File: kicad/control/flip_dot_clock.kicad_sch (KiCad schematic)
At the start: 36 parts, among them J1 Conn_01x02_Male, J2 Conn_02x08_Odd_Even, J3 Conn_01x05_Male, U1 NUCLEO-F303K8-HEADER, U10 Small_7_Seg_FlipDot_Module, U2 SLC03B-05, U3 NCV7719, U4 Small_7_Seg_FlipDot_Module, U5 NCV7719, U6 Small_7_Seg_FlipDot_Module, U7 NCV7719, U8 Small_7_Seg_FlipDot_Module, U9 NCV7719

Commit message: kicad update
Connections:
- net +5V: now also J2.10 (Pin_10); no longer J2.6 (Pin_6)
- net GND: now also J2.14 (Pin_14); no longer J2.10 (Pin_10)

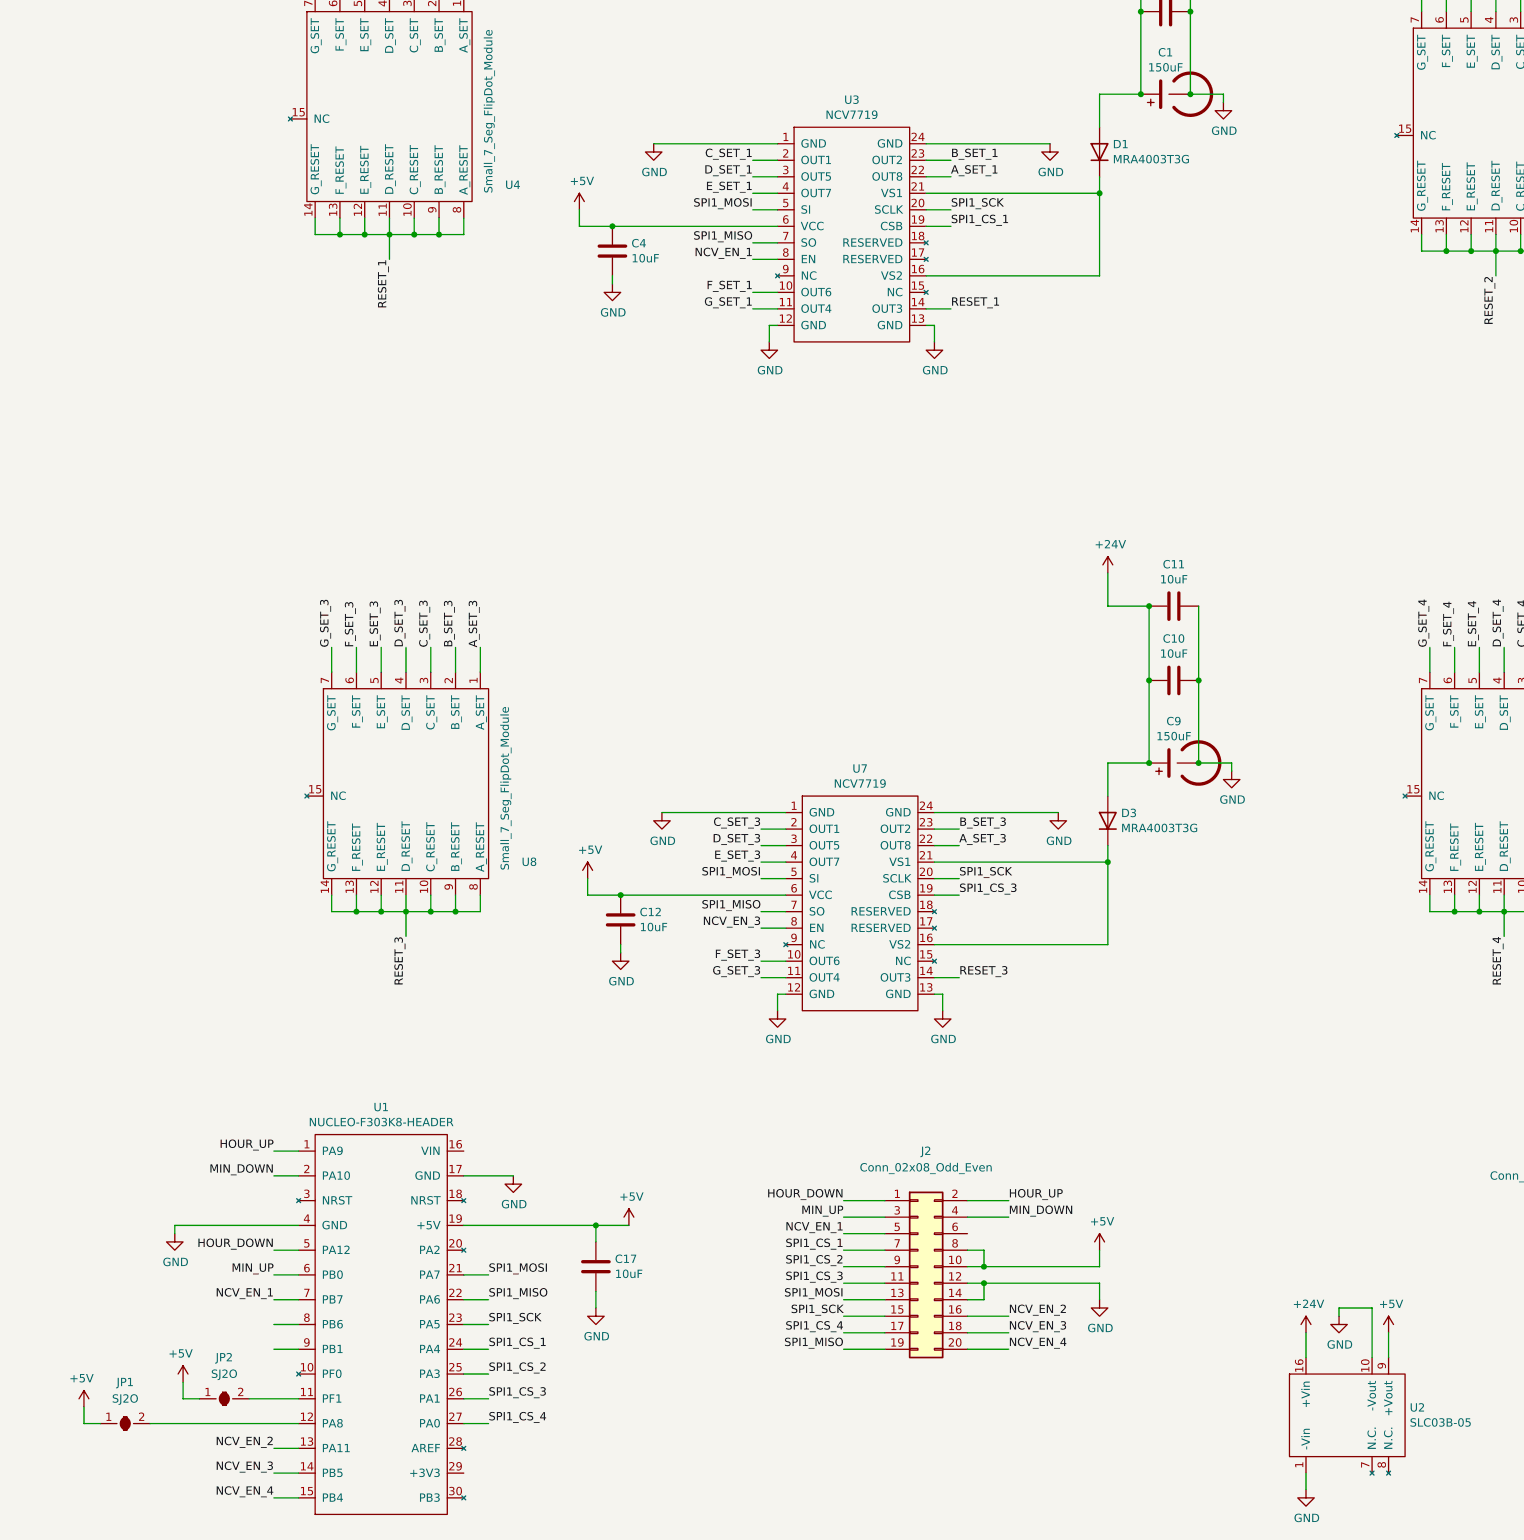
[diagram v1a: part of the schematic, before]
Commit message: add digit holder ground planes
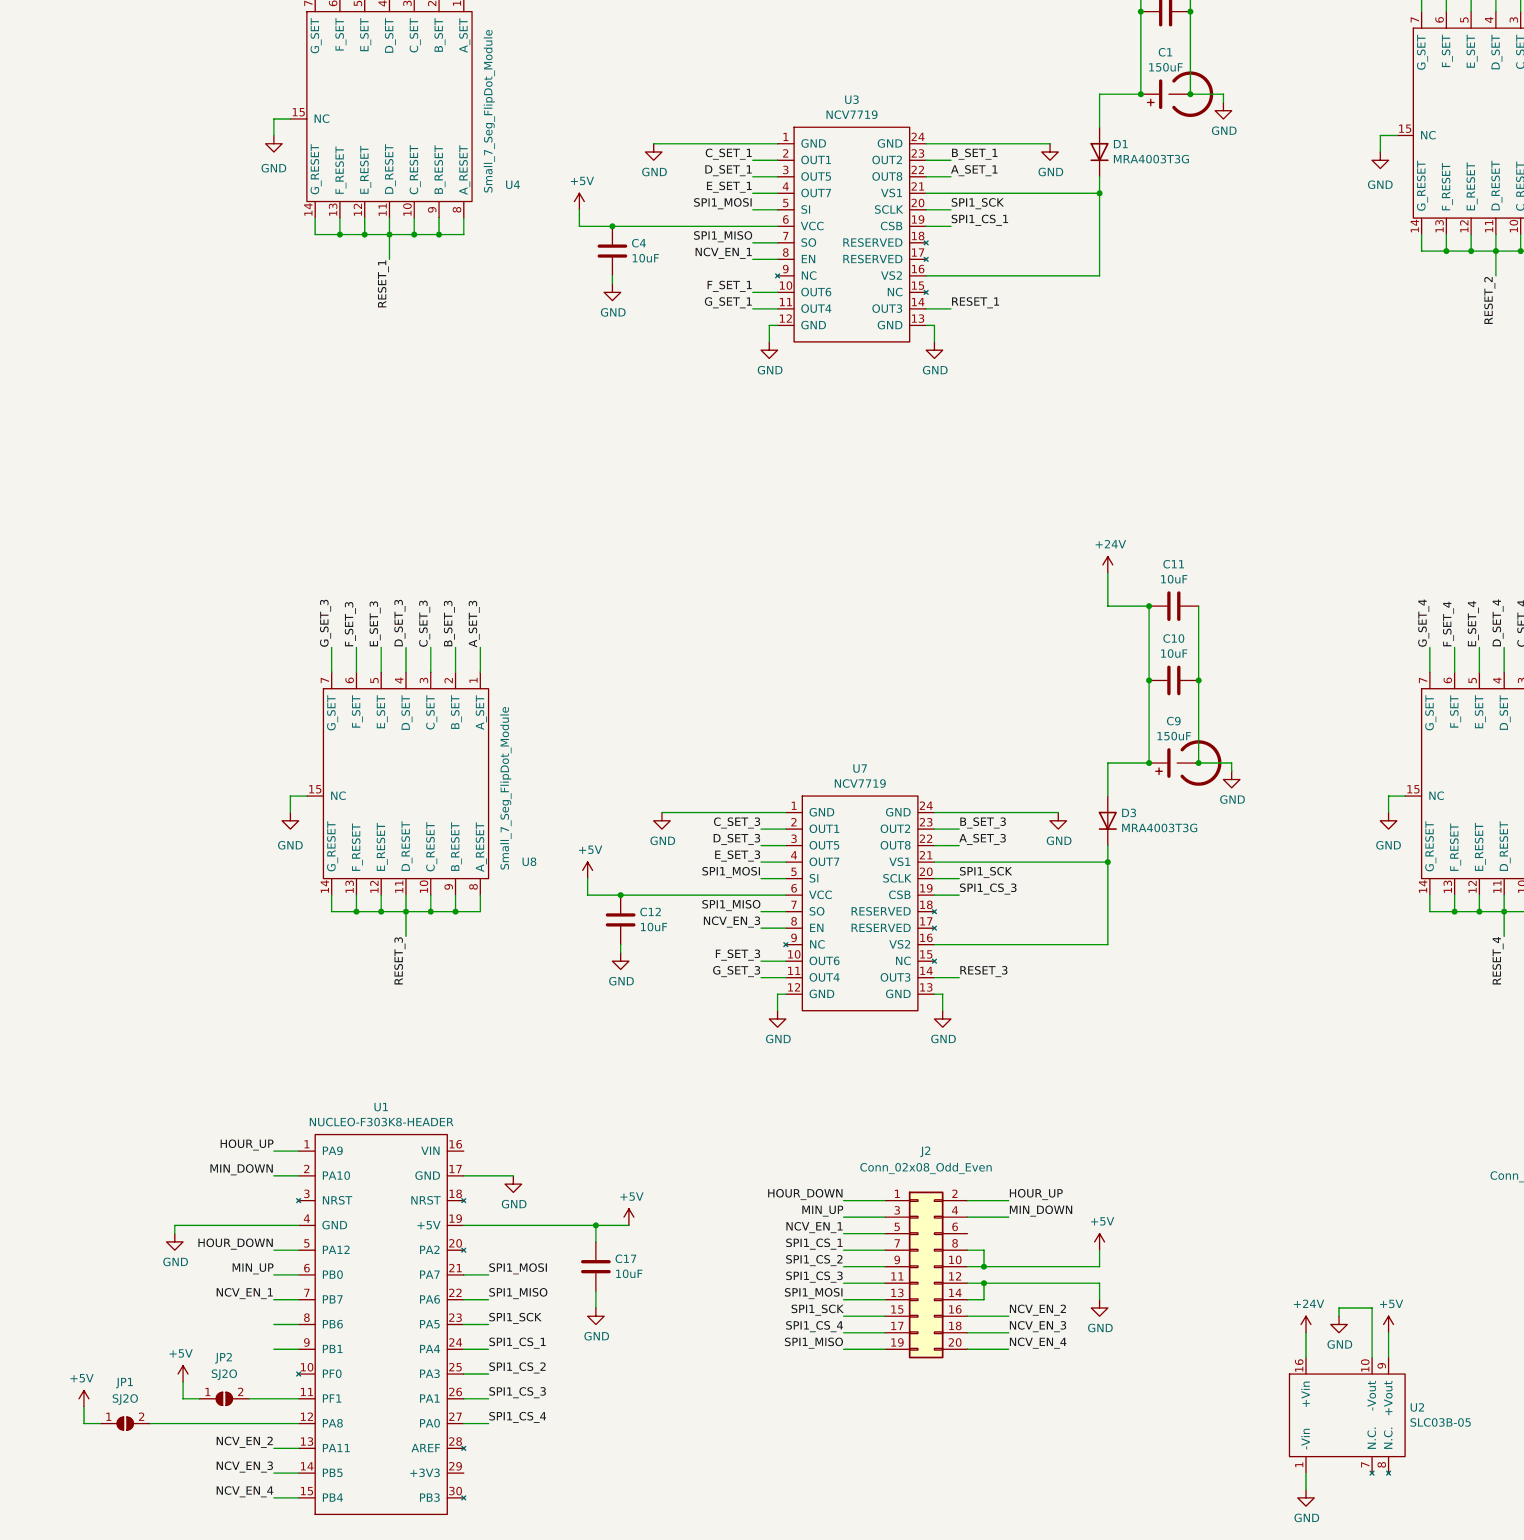
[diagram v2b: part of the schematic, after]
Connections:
- net GND: now also U10.15 (NC), U4.15 (NC), U6.15 (NC), U8.15 (NC)
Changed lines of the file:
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@@
+    (stroke (width 0) (type default))
+  )
+  (wire (pts (xy 86.36 163.83) (xy 88.9 163.83))
     (stroke (width 0) (type default))
   )
@@
     (stroke (width 0) (type default))
   )
+  (wire (pts (xy 254 62.23) (xy 256.54 62.23))
+    (stroke (width 0) (type default))
+  )
   (wire (pts (xy 328.93 67.31) (xy 332.74 67.31))
     (stroke (width 0) (type default))
@@
     (stroke (width 0) (type default))
   )
+  (wire (pts (xy 83.82 62.23) (xy 83.82 59.69))
+    (stroke (width 0) (type default))
+  )
   (wire (pts (xy 104.14 144.78) (xy 104.14 140.97))
     (stroke (width 0) (type default))
@@
     (stroke (width 0) (type default))
   )
+  (wire (pts (xy 86.36 166.37) (xy 86.36 163.83))
+    (stroke (width 0) (type default))
+  )
   (wire (pts (xy 187.96 68.58) (xy 184.15 68.58))
     (stroke (width 0) (type default))
@@
     (stroke (width 0) (type default))
   )
+  (wire (pts (xy 255.27 163.83) (xy 257.81 163.83))
+    (stroke (width 0) (type default))
+  )
   (wire (pts (xy 280.67 181.61) (xy 280.67 179.07))
     (stroke (width 0) (type default))
@@
     (stroke (width 0) (type default))
   )
+  (wire (pts (xy 255.27 166.37) (xy 255.27 163.83))
+    (stroke (width 0) (type default))
+  )
   (wire (pts (xy 396.24 44.45) (xy 396.24 33.02))
     (stroke (width 0) (type default))
@@
     (stroke (width 0) (type default))
   )
+  (wire (pts (xy 254 64.77) (xy 254 62.23))
+    (stroke (width 0) (type default))
+  )
   (wire (pts (xy 355.6 74.93) (xy 359.41 74.93))
     (stroke (width 0) (type default))
@@
   )
   (wire (pts (xy 261.62 144.78) (xy 261.62 140.97))
+    (stroke (width 0) (type default))
+  )
+  (wire (pts (xy 83.82 59.69) (xy 86.36 59.69))
     (stroke (width 0) (type default))
   )
@@
     (pin "1")
   )
-  (symbol (lib_id "mio:Small_7_Seg_FlipDot_Module") (at 271.78 43.18 0) (unit 1)
+  (symbol (lib_name "Small_7_Seg_FlipDot_Module_2") (lib_id "mio:Small_7_Seg_FlipDot_Module") (at 271.78 43.18 0) (unit 1)
     (in_bom yes) (on_board yes)
     (property "Reference" "U6" (id 0) (at 289.56 72.39 0)
@@
     (pin "9")
   )
-  (symbol (lib_id "mio:Small_7_Seg_FlipDot_Module") (at 273.05 144.78 0) (unit 1)
+  (symbol (lib_name "Small_7_Seg_FlipDot_Module_1") (lib_id "mio:Small_7_Seg_FlipDot_Module") (at 273.05 144.78 0) (unit 1)
     (in_bom yes) (on_board yes)
     (property "Reference" "U10" (id 0) (at 290.83 173.99 0)
@@
     (pin "1")
   )
-  (symbol (lib_id "mio:Small_7_Seg_FlipDot_Module") (at 104.14 144.78 0) (unit 1)
+  (symbol (lib_name "Small_7_Seg_FlipDot_Module_3") (lib_id "mio:Small_7_Seg_FlipDot_Module") (at 104.14 144.78 0) (unit 1)
     (in_bom yes) (on_board yes)
     (property "Reference" "U8" (id 0) (at 121.92 173.99 0)
@@
     (pin "1")
   )
+  (symbol (lib_id "power:GND") (at 83.82 62.23 0) (unit 1)
+    (in_bom yes) (on_board yes) (fields_autoplaced)
+    (property "Reference" "#PWR?" (id 0) (at 83.82 68.58 0)
+      (effects (font (size 1.27 1.27)) hide)
+    )
+    (property "Value" "GND" (id 1) (at 83.82 67.31 0)
+      (effects (font (size 1.27 1.27)))
+    )
+    (property "Footprint" "" (id 2) (at 83.82 62.23 0)
+      (effects (font (size 1.27 1.27)) hide)
+    )
+    (property "Datasheet" "" (id 3) (at 83.82 62.23 0)
+      (effects (font (size 1.27 1.27)) hide)
+    )
+    (pin "1")
+  )
   (symbol (lib_id "power:+5V") (at 69.85 254 0) (mirror y) (unit 1)
     (in_bom yes) (on_board yes)
@@
     (pin "2")
   )
+  (symbol (lib_id "power:GND") (at 254 64.77 0) (unit 1)
+    (in_bom yes) (on_board yes) (fields_autoplaced)
+    (property "Reference" "#PWR?" (id 0) (at 254 71.12 0)
+      (effects (font (size 1.27 1.27)) hide)
+    )
+    (property "Value" "GND" (id 1) (at 254 69.85 0)
+      (effects (font (size 1.27 1.27)))
+    )
+    (property "Footprint" "" (id 2) (at 254 64.77 0)
+      (effects (font (size 1.27 1.27)) hide)
+    )
+    (property "Datasheet" "" (id 3) (at 254 64.77 0)
+      (effects (font (size 1.27 1.27)) hide)
+    )
+    (pin "1")
+  )
   (symbol (lib_id "power:+5V") (at 302.26 74.93 0) (unit 1)
     (in_bom yes) (on_board yes)
@@
     )
     (property "Datasheet" "" (id 3) (at 302.26 74.93 0)
+      (effects (font (size 1.27 1.27)) hide)
+    )
+    (pin "1")
+  )
+  (symbol (lib_id "power:GND") (at 86.36 166.37 0) (unit 1)
+    (in_bom yes) (on_board yes) (fields_autoplaced)
+    (property "Reference" "#PWR?" (id 0) (at 86.36 172.72 0)
+      (effects (font (size 1.27 1.27)) hide)
+    )
+    (property "Value" "GND" (id 1) (at 86.36 171.45 0)
+      (effects (font (size 1.27 1.27)))
+    )
+    (property "Footprint" "" (id 2) (at 86.36 166.37 0)
+      (effects (font (size 1.27 1.27)) hide)
+    )
+    (property "Datasheet" "" (id 3) (at 86.36 166.37 0)
       (effects (font (size 1.27 1.27)) hide)
     )
@@
     (pin "2")
   )
+  (symbol (lib_id "power:GND") (at 255.27 166.37 0) (unit 1)
+    (in_bom yes) (on_board yes) (fields_autoplaced)
+    (property "Reference" "#PWR?" (id 0) (at 255.27 172.72 0)
+      (effects (font (size 1.27 1.27)) hide)
+    )
+    (property "Value" "GND" (id 1) (at 255.27 171.45 0)
+      (effects (font (size 1.27 1.27)))
+    )
+    (property "Footprint" "" (id 2) (at 255.27 166.37 0)
+      (effects (font (size 1.27 1.27)) hide)
+    )
+    (property "Datasheet" "" (id 3) (at 255.27 166.37 0)
+      (effects (font (size 1.27 1.27)) hide)
+    )
+    (pin "1")
+  )
   (symbol (lib_id "power:GND") (at 133.35 242.57 0) (unit 1)
     (in_bom yes) (on_board yes)
@@
       (reference "#PWR0134") (unit 1) (value "GND") (footprint "")
     )
+    (path "/795741d0-85b8-4f07-9fad-64977b7593b3"
+      (reference "#PWR?") (unit 1) (value "GND") (footprint "")
+    )
+    (path "/8e050dd7-51c3-4022-99d1-263f3d2804f7"
+      (reference "#PWR?") (unit 1) (value "GND") (footprint "")
+    )
+    (path "/9faa18e3-d506-4f2f-9547-fdb3f28a5c69"
+      (reference "#PWR?") (unit 1) (value "GND") (footprint "")
+    )
+    (path "/e5767851-16b2-4e9c-863a-a06c33998d8d"
+      (reference "#PWR?") (unit 1) (value "GND") (footprint "")
+    )
     (path "/00000000-0000-0000-0000-000061f1c429"
